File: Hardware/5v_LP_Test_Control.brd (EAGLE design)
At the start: 12.7 x 10.1 mm, 7 parts, among them J2 CONN_3, U1 TLV61220DBV

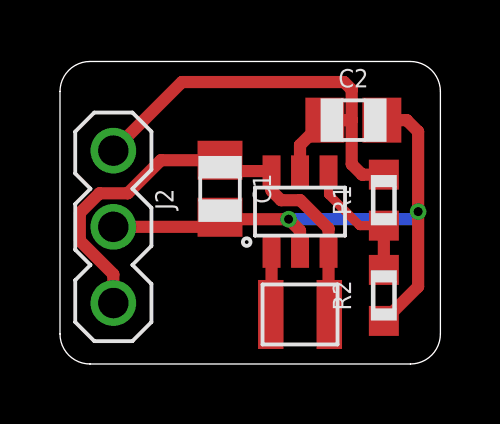
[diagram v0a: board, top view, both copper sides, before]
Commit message: Updated test boards for VolteraV1
Attempted to maximize compatibility with Voltera V1 system
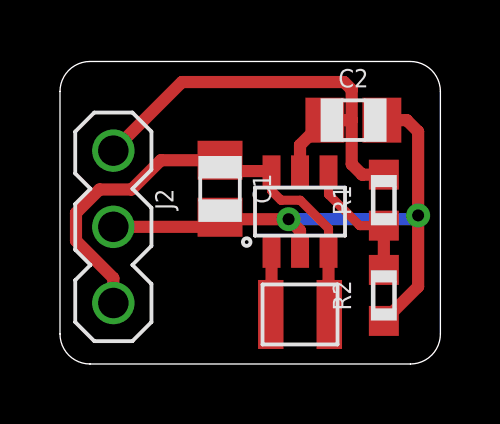
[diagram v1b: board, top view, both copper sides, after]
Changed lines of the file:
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@@
 <drawing>
 <settings>
-<setting alwaysvectorfont="no"/>
+<setting alwaysvectorfont="yes"/>
 <setting verticaltext="up"/>
 </settings>
@@
 </class>
 </classes>
-<designrules name="oshpark-2layer *">
-<description language="en">&lt;b&gt;OSH Park Design Rules&lt;/b&gt;
+<designrules name="voltera-dru">
+<description language="de">&lt;b&gt;EAGLE Design Rules&lt;/b&gt;
 &lt;p&gt;
-Please make sure your boards conform to these design rules.
+Die Standard-Design-Rules sind so gewählt, dass sie für
+die meisten Anwendungen passen. Sollte ihre Platine
+besondere Anforderungen haben, treffen Sie die erforderlichen
+Einstellungen hier und speichern die Design Rules unter
+einem neuen Namen ab.</description>
+<description language="en">&lt;b&gt;VOLTERA V-ONE Design Rules&lt;/b&gt;
+&lt;p&gt;
+These design rules are intended to identify common sources of printing errors when printing a circuit with the Voltera V-One. &lt;b&gt;Always thoroughly check your design in the V-One software print preview before printing!
+&lt;p&gt;&lt;b&gt;COPPER POURS:&lt;/b&gt; Use Hatch planes, or replace with a trace.
+&lt;br&gt;&lt;b&gt;BOARD SIZE:&lt;/b&gt; Maximum 4x5 inches.
 &lt;/p&gt;
 &lt;p&gt;
-Note, that not all DRC settings must be set by the manufacturer. Several can be adjusted for the design, including those listed on our docs page here.
-&lt;a href=&quot;http://docs.oshpark.com/design-tools/eagle/design-rules-files/&quot;&gt;Adjustable Settings&lt;/a&gt;
-&lt;/p&gt;</description>
+V1.0 2018-04-18
+&lt;ul&gt;
+&lt;li&gt;Min trace width / spacing set to 10 mil.
+&lt;li&gt;Recommended minimum via drill diameter 0.4mm.
+&lt;li&gt;Minimum annular ring for via/pad 0.2mm.
+&lt;li&gt;Changed restring value to 0 for rivets.
+&lt;/ul&gt;</description>
 <param name="layerSetup" value="(1*16)"/>
-<param name="mtCopper" value="0.035559375mm 0.0356mm 0.0356mm 0.0356mm 0.0356mm 0.0356mm 0.0356mm 0.0356mm 0.0356mm 0.0356mm 0.0356mm 0.0356mm 0.0356mm 0.0356mm 0.0356mm 0.035559375mm"/>
-<param name="mtIsolate" value="1.6mm 0.1499mm 0.2007mm 0.1499mm 0.2007mm 0.1499mm 0.2007mm 0.1499mm 0.2007mm 0.1499mm 0.2007mm 0.1499mm 0.2007mm 0.1499mm 0.2007mm"/>
-<param name="mdWireWire" value="8mil"/>
-<param name="mdWirePad" value="8mil"/>
-<param name="mdWireVia" value="8mil"/>
-<param name="mdPadPad" value="8mil"/>
-<param name="mdPadVia" value="8mil"/>
-<param name="mdViaVia" value="6mil"/>
-<param name="mdSmdPad" value="6mil"/>
-<param name="mdSmdVia" value="6mil"/>
-<param name="mdSmdSmd" value="6mil"/>
+<param name="mtCopper" value="0.035mm 0.035mm 0.035mm 0.035mm 0.035mm 0.035mm 0.035mm 0.035mm 0.035mm 0.035mm 0.035mm 0.035mm 0.035mm 0.035mm 0.035mm 0.035mm"/>
+<param name="mtIsolate" value="1.5mm 0.15mm 0.2mm 0.15mm 0.2mm 0.15mm 0.2mm 0.15mm 0.2mm 0.15mm 0.2mm 0.15mm 0.2mm 0.15mm 0.2mm"/>
+<param name="mdWireWire" value="10mil"/>
+<param name="mdWirePad" value="10mil"/>
+<param name="mdWireVia" value="0.6mm"/>
+<param name="mdPadPad" value="0.6mm"/>
+<param name="mdPadVia" value="0.6mm"/>
+<param name="mdViaVia" value="0.6mm"/>
+<param name="mdSmdPad" value="0mil"/>
+<param name="mdSmdVia" value="0mil"/>
+<param name="mdSmdSmd" value="0mil"/>
 <param name="mdViaViaSameLayer" value="8mil"/>
 <param name="mnLayersViaInSmd" value="2"/>
-<param name="mdCopperDimension" value="15mil"/>
-<param name="mdDrill" value="6mil"/>
+<param name="mdCopperDimension" value="0mil"/>
+<param name="mdDrill" value="0.8mm"/>
 <param name="mdSmdStop" value="0mil"/>
-<param name="msWidth" value="8mil"/>
-<param name="msDrill" value="10mil"/>
-<param name="msMicroVia" value="10mil"/>
+<param name="msWidth" value="10mil"/>
+<param name="msDrill" value="0.4mm"/>
+<param name="msMicroVia" value="9.99mm"/>
 <param name="msBlindViaRatio" value="0.5"/>
-<param name="rvPadTop" value="0.25"/>
-<param name="rvPadInner" value="0.25"/>
-<param name="rvPadBottom" value="0.25"/>
-<param name="rvViaOuter" value="0.25"/>
-<param name="rvViaInner" value="0.25"/>
-<param name="rvMicroViaOuter" value="0.25"/>
-<param name="rvMicroViaInner" value="0.25"/>
-<param name="rlMinPadTop" value="5mil"/>
+<param name="rvPadTop" value="0"/>
+<param name="rvPadInner" value="0"/>
+<param name="rvPadBottom" value="0"/>
+<param name="rvViaOuter" value="0"/>
+<param name="rvViaInner" value="0"/>
+<param name="rvMicroViaOuter" value="0"/>
+<param name="rvMicroViaInner" value="0"/>
+<param name="rlMinPadTop" value="0.2mm"/>
 <param name="rlMaxPadTop" value="20mil"/>
-<param name="rlMinPadInner" value="5mil"/>
+<param name="rlMinPadInner" value="10mil"/>
 <param name="rlMaxPadInner" value="20mil"/>
-<param name="rlMinPadBottom" value="5mil"/>
+<param name="rlMinPadBottom" value="0.2mm"/>
 <param name="rlMaxPadBottom" value="20mil"/>
-<param name="rlMinViaOuter" value="5mil"/>
+<param name="rlMinViaOuter" value="0.2mm"/>
 <param name="rlMaxViaOuter" value="20mil"/>
-<param name="rlMinViaInner" value="5mil"/>
+<param name="rlMinViaInner" value="10mil"/>
 <param name="rlMaxViaInner" value="20mil"/>
-<param name="rlMinMicroViaOuter" value="5mil"/>
+<param name="rlMinMicroViaOuter" value="4mil"/>
 <param name="rlMaxMicroViaOuter" value="20mil"/>
-<param name="rlMinMicroViaInner" value="5mil"/>
+<param name="rlMinMicroViaInner" value="4mil"/>
 <param name="rlMaxMicroViaInner" value="20mil"/>
 <param name="psTop" value="-1"/>
@@
 <param name="mvStopFrame" value="1"/>
 <param name="mvCreamFrame" value="0"/>
-<param name="mlMinStopFrame" value="2.5mil"/>
-<param name="mlMaxStopFrame" value="2.5mil"/>
+<param name="mlMinStopFrame" value="4mil"/>
+<param name="mlMaxStopFrame" value="4mil"/>
 <param name="mlMinCreamFrame" value="0mil"/>
 <param name="mlMaxCreamFrame" value="0mil"/>
@@
 <param name="dpMaxLengthDifference" value="10mm"/>
 <param name="dpGapFactor" value="2.5"/>
-<param name="checkAngle" value="0"/>
+<param name="checkAngle" value="1"/>
 <param name="checkFont" value="1"/>
 <param name="checkRestrict" value="1"/>
@@
 <wire x1="8.001" y1="3.73" x2="8.001" y2="4.445" width="0.4064" layer="1"/>
 <wire x1="8.001" y1="4.445" x2="7.62" y2="4.826" width="0.4064" layer="1"/>
-<via x="7.62" y="4.826" extent="1-16" drill="0.3"/>
+<via x="7.62" y="4.826" extent="1-16" drill="0.4"/>
 <wire x1="5.334" y1="4.892" x2="5.4" y2="4.826" width="0.4064" layer="1"/>
 <wire x1="5.4" y1="4.826" x2="7.62" y2="4.826" width="0.4064" layer="1"/>
 <wire x1="10.729" y1="8.128" x2="11.557" y2="8.128" width="0.4064" layer="1"/>
 <wire x1="11.557" y1="8.128" x2="11.938" y2="7.747" width="0.4064" layer="1"/>
-<wire x1="11.938" y1="7.747" x2="11.938" y2="5.08" width="0.4064" layer="1"/>
-<wire x1="11.938" y1="5.08" x2="11.938" y2="2.579" width="0.4064" layer="1"/>
+<wire x1="11.938" y1="7.747" x2="11.938" y2="4.953" width="0.4064" layer="1"/>
+<wire x1="11.938" y1="4.953" x2="11.938" y2="2.579" width="0.4064" layer="1"/>
 <wire x1="11.938" y1="2.579" x2="10.795" y2="1.436" width="0.4064" layer="1"/>
-<wire x1="7.62" y1="4.826" x2="11.811" y2="4.826" width="0.4064" layer="16"/>
-<wire x1="11.811" y1="4.826" x2="11.938" y2="5.08" width="0.4064" layer="16"/>
-<via x="11.938" y="5.08" extent="1-16" drill="0.3"/>
+<wire x1="7.62" y1="4.826" x2="11.8745" y2="4.826" width="0.4064" layer="16"/>
+<wire x1="11.8745" y1="4.826" x2="11.938" y2="4.953" width="0.4064" layer="16"/>
+<via x="11.938" y="4.953" extent="1-16" drill="0.4"/>
 <contactref element="J2" pad="2"/>
 <wire x1="5.334" y1="4.892" x2="5.014" y2="4.572" width="0.4064" layer="1"/>
@@
 <wire x1="5.334" y1="6.792" x2="5.696" y2="6.43" width="0.4064" layer="1"/>
 <wire x1="5.696" y1="6.43" x2="7.051" y2="6.43" width="0.4064" layer="1"/>
-<wire x1="7.051" y1="6.43" x2="7.051" y2="5.776" width="0.4064" layer="1"/>
-<wire x1="7.3684" y1="5.4586" x2="8.0090375" y2="5.4586" width="0.4064" layer="1"/>
-<wire x1="8.0090375" y1="5.4586" x2="8.951" y2="4.5166375" width="0.4064" layer="1"/>
-<wire x1="7.051" y1="5.776" x2="7.3684" y2="5.4586" width="0.4064" layer="1"/>
-<wire x1="8.951" y1="4.5166375" x2="8.951" y2="3.73" width="0.4064" layer="1"/>
+<wire x1="7.051" y1="6.43" x2="7.051" y2="5.776" width="0.3048" layer="1"/>
+<wire x1="7.3684" y1="5.4586" x2="8.0090375" y2="5.4586" width="0.3048" layer="1"/>
+<wire x1="8.0090375" y1="5.4586" x2="8.951" y2="4.5166375" width="0.3048" layer="1"/>
+<wire x1="7.051" y1="5.776" x2="7.3684" y2="5.4586" width="0.3048" layer="1"/>
+<wire x1="8.951" y1="4.5166375" x2="8.951" y2="3.73" width="0.3048" layer="1"/>
 <wire x1="8.951" y1="3.73" x2="8.951" y2="1.676" width="0.4064" layer="1"/>
 <wire x1="8.951" y1="1.676" x2="8.976" y2="1.651" width="0.4064" layer="1"/>
 <contactref element="J2" pad="3"/>
 <wire x1="5.334" y1="6.792" x2="3.363" y2="6.792" width="0.4064" layer="1"/>
-<wire x1="1.31506875" y1="5.6896" x2="0.6604" y2="5.03493125" width="0.4064" layer="1"/>
-<wire x1="0.6604" y1="5.03493125" x2="0.6604" y2="4.10906875" width="0.4064" layer="1"/>
-<wire x1="1.778" y1="2.99146875" x2="1.778" y2="2.032" width="0.4064" layer="1"/>
-<wire x1="2.2606" y1="5.6896" x2="1.31506875" y2="5.6896" width="0.4064" layer="1"/>
-<wire x1="0.6604" y1="4.10906875" x2="1.778" y2="2.99146875" width="0.4064" layer="1"/>
-<wire x1="3.363" y1="6.792" x2="2.2606" y2="5.6896" width="0.4064" layer="1"/>
+<wire x1="1.31506875" y1="5.8166" x2="0.5334" y2="5.03493125" width="0.4064" layer="1"/>
+<wire x1="0.5334" y1="5.03493125" x2="0.5334" y2="4.10906875" width="0.4064" layer="1"/>
+<wire x1="1.778" y1="2.86446875" x2="1.778" y2="2.032" width="0.4064" layer="1"/>
+<wire x1="2.3876" y1="5.8166" x2="1.31506875" y2="5.8166" width="0.4064" layer="1"/>
+<wire x1="0.5334" y1="4.10906875" x2="1.778" y2="2.86446875" width="0.4064" layer="1"/>
+<wire x1="3.363" y1="6.792" x2="2.3876" y2="5.8166" width="0.4064" layer="1"/>
 </signal>
 <signal name="N$5">
